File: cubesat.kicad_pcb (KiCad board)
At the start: 2 copper layers, 7 parts, among them U1 MCP9808_MSOP, U2 MPU-6050

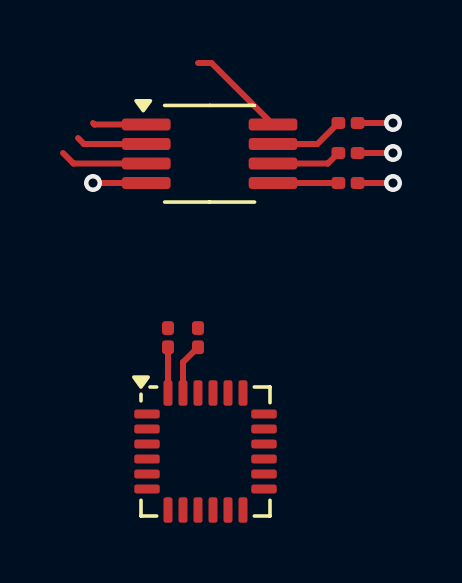
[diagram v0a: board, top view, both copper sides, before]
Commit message: add mpu schéma
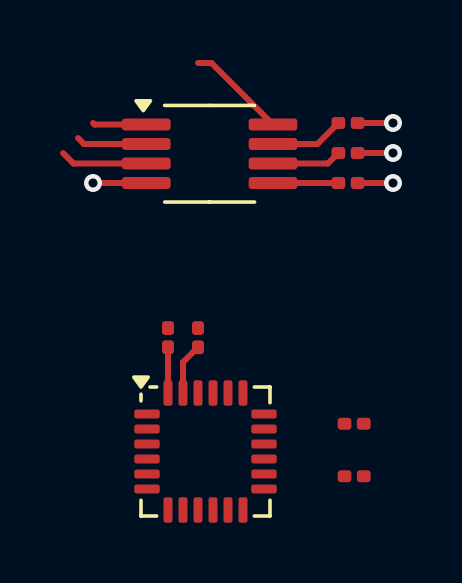
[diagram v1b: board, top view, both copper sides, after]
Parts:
- added R6: 4.7k, Resistor_SMD:R_0201_0603Metric, F.Cu at (53.7, 72.0)
- added R7: 4.7k, Resistor_SMD:R_0201_0603Metric, F.Cu at (53.7, 73.8)
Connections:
- R4 pad 2: Net-(R4-Pad2) -> +3V3
- R5 pad 1: Net-(R4-Pad2) -> +3V3
- U2 pad 10: unconnected-(U2-REGOUT-Pad10) -> Net-(U2-REGOUT)
- U2 pad 13: unconnected-(U2-VDD-Pad13) -> +3V3
- U2 pad 20: unconnected-(U2-CPOUT-Pad20) -> Net-(U2-CPOUT)
- U2 pad 6: unconnected-(U2-AUX_DA-Pad6) -> Net-(U2-AUX_DA)
- U2 pad 7: unconnected-(U2-AUX_CL-Pad7) -> Net-(U2-AUX_CL)
- U2 pad 8: unconnected-(U2-VLOGIC-Pad8) -> +3V3
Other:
- board text added: "R5"
